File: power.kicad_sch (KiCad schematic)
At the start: 7 parts

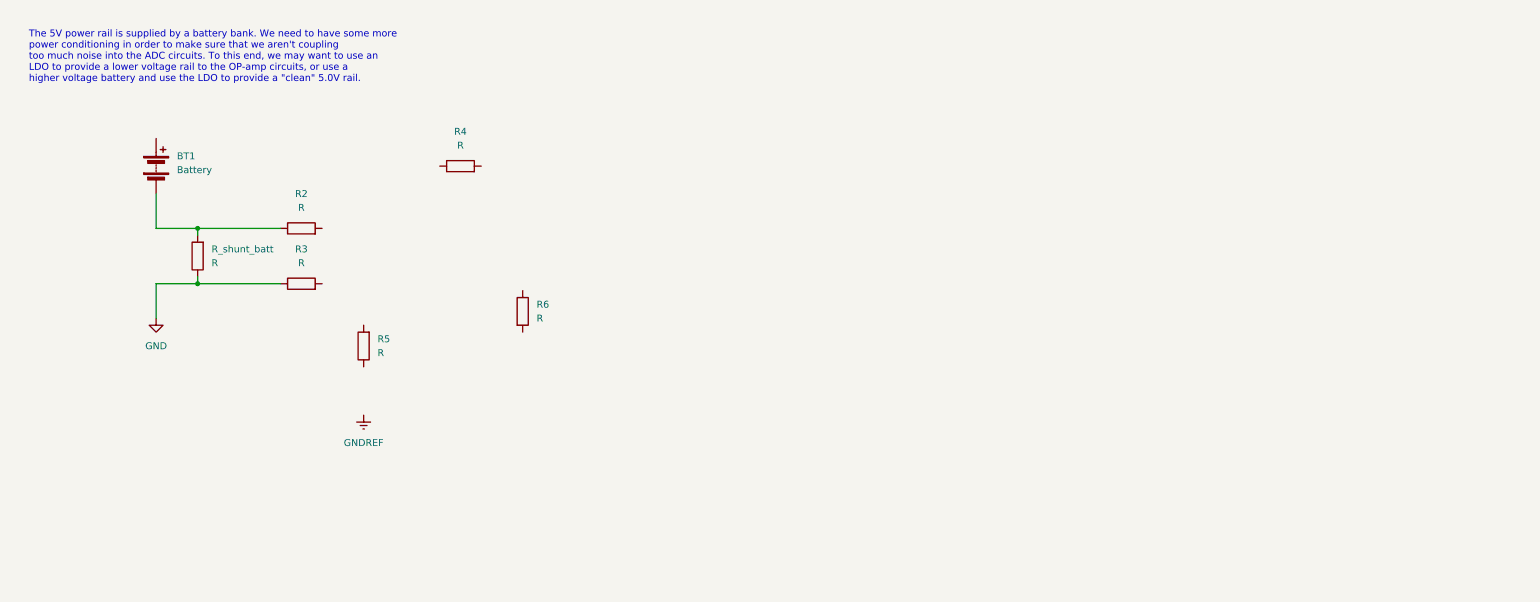
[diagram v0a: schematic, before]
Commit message: Split the sensor modules into a 4 and 8 port version. Fleshed out the power module a bit more. Started adding sensor board connectors to the root schematic and started pulling out sensor boards to their own, separate module. Began wiring up the root schematic to get my bearings a bit.
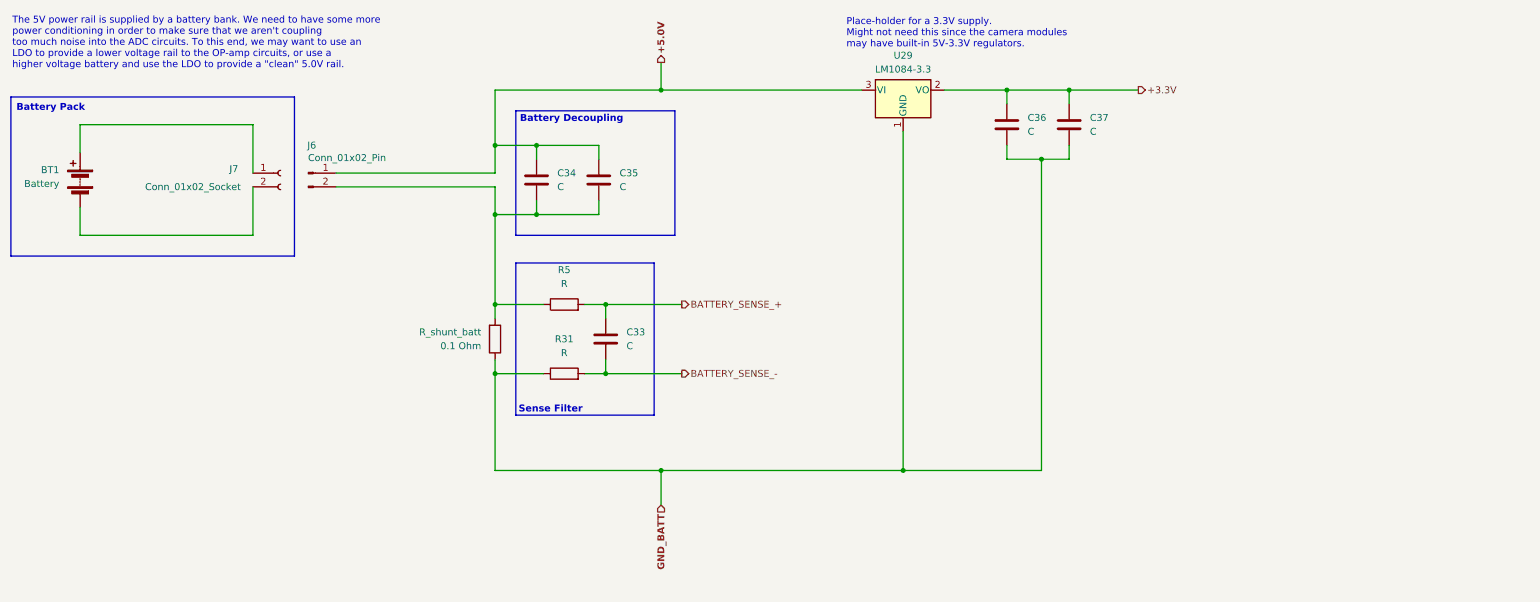
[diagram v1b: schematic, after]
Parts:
- removed R2, R3, R4, R6: R, symbol Device:R
- added C33, C34, C35, C36, C37: C, symbol Device:C
- added J6: Conn_01x02_Pin, symbol Connector:Conn_01x02_Pin
- added J7: Conn_01x02_Socket, symbol Connector:Conn_01x02_Socket
- added R31: R, symbol Device:R
- added U29: LM1084-3.3, symbol Regulator_Linear:LM1084-3.3
- R_shunt_batt: value R -> 0.1 Ohm
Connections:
- net at R_shunt_batt.2: now also R5.1, C34.2, C35.2, J6.2 (Pin_2); no longer BT1.2 (-)
- net at BT1.1 (+): now also J7.1 (Pin_1)
- net BATTERY_SENSE_+: now reaches R5.2
- net BATTERY_SENSE_+: now also C33.1
- net GND renamed GND_BATT
- net GND_BATT: now also C36.2, C37.2, R31.1, U29.1 (GND)
- new net: BT1.2 (-), J7.2 (Pin_2)
- new net +3.3V: C36.1, C37.1, U29.2 (VO)
- new net +5.0V: C34.1, C35.1, J6.1 (Pin_1), U29.3 (VI)
- new net BATTERY_SENSE_-: C33.2, R31.2
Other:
- note added: "Battery Decoupling"
- note added: "Battery Pack"
- note added: "Place-holder for a 3.3V supply. Might not need this since the camera modules may have built-in 5V-3.3V regulators."
- note added: "Sense Filter"
- moved on the sheet: BT1, R_shunt_batt

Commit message: More notes and comments Cleaned up some signal lines Compacted the decoupling sections Added Turbidity placeholder
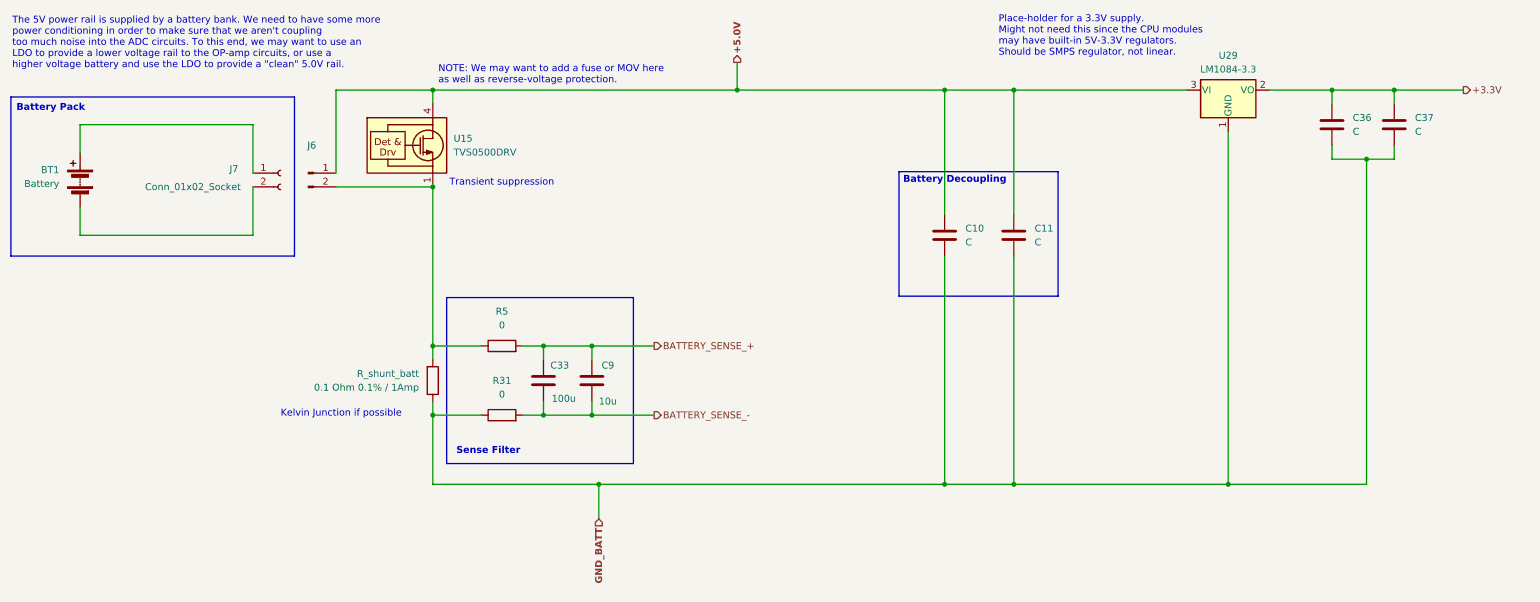
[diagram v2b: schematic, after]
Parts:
- removed C34, C35: C, symbol Device:C
- added C10, C11: C, symbol Device:C
- added C9: 10u, symbol Device:C
- added U15: TVS0500DRV, Package_SON:WSON-6-1EP_2x2mm_P0.65mm_EP1x1.6mm, symbol Power_Protection:TVS0500DRV
- C33: value C -> 100u
- R31, R5: value R -> 0
- R_shunt_batt: value 0.1 Ohm -> 0.1 Ohm 0.1% / 1Amp
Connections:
- net +5.0V: now also C10.1, C11.1, U15.4 (IN), U15.5 (IN), U15.6 (IN)
- net BATTERY_SENSE_+: now also C9.1
- net BATTERY_SENSE_-: now also C9.2
- net GND_BATT: now also C10.2, C11.2
- net at J6.2 (Pin_2), R5.1, R_shunt_batt.2: now also U15.1 (GND), U15.2 (GND), U15.3 (GND), U15.7 (GND)
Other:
- note added: "Kelvin Junction if possible"
- note added: "NOTE: We may want to add a fuse or MOV here as well as reverse-voltage protection."
- note added: "Place-holder for a 3.3V supply. Might not need this since the CPU modules may have built-in 5V-3.3V regulators. Should be SMPS regulator, not linear."
- note added: "Transient suppression"
- note removed: "Place-holder for a 3.3V supply. Might not need this since the camera modules may have built-in 5V-3.3V regulators."
- moved on the sheet: C33, C36, C37, R31, R5, R_shunt_batt, U29

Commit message: Cleaned up a bit Added a SPDT to calibrate signal on the base board Added PTC and MOV to power section
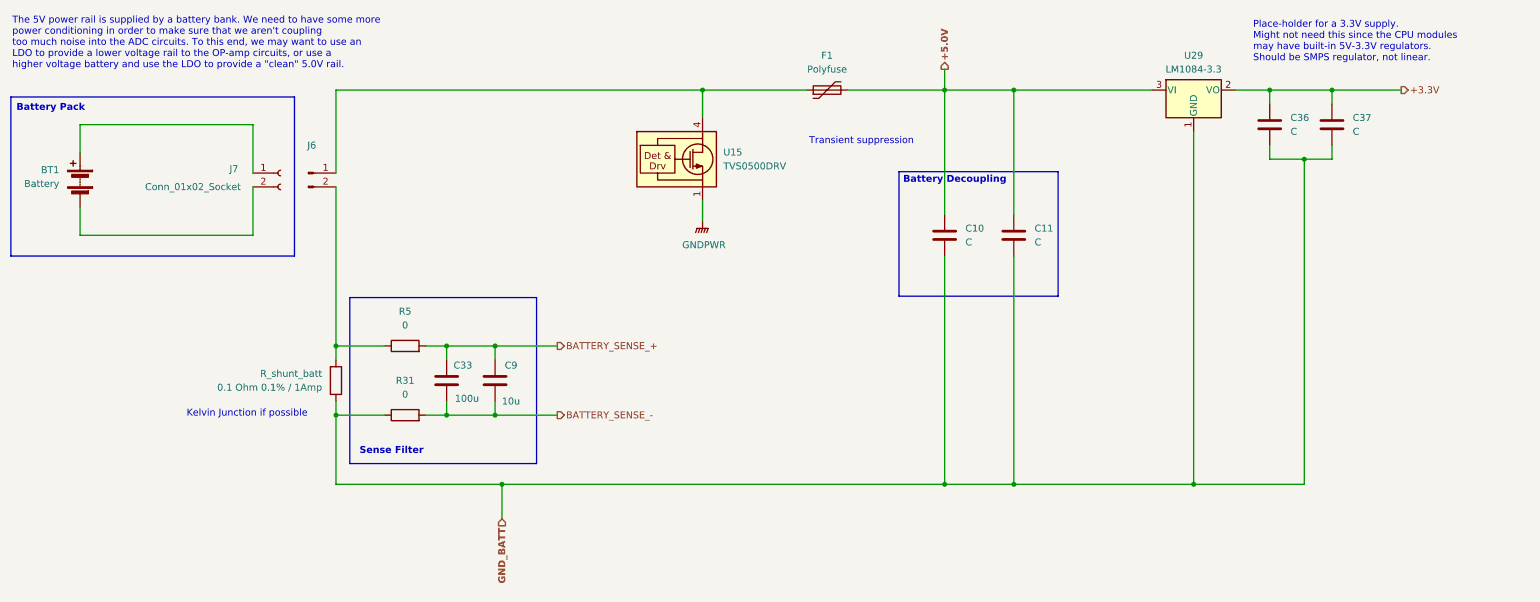
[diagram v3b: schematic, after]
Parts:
- added F1: Polyfuse, symbol Device:Polyfuse
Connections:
- net +5.0V: now also F1.2; no longer J6.1 (Pin_1), U15.4 (IN), U15.5 (IN), U15.6 (IN)
- net GNDPWR: now reaches U15.1 (GND), U15.2 (GND), U15.3 (GND), U15.7 (GND)
- net GNDPWR: no longer J6.2 (Pin_2), R5.1, R_shunt_batt.2
- new net: J6.2 (Pin_2), R5.1, R_shunt_batt.2
- new net: F1.1, J6.1 (Pin_1), U15.4 (IN), U15.5 (IN), U15.6 (IN)
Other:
- note removed: "NOTE: We may want to add a fuse or MOV here as well as reverse-voltage protection."
- moved on the sheet: C33, C36, C37, C9, R31, R5, R_shunt_batt, U29

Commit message: Began assigning footprints Cleaned up some of the signalling and added the full prototype sensor suite Added a header for the Atlas Scientific carrier board Added some test points and jumpers Cleaned up the power section Started work on the CPU signal assignment and header sockets
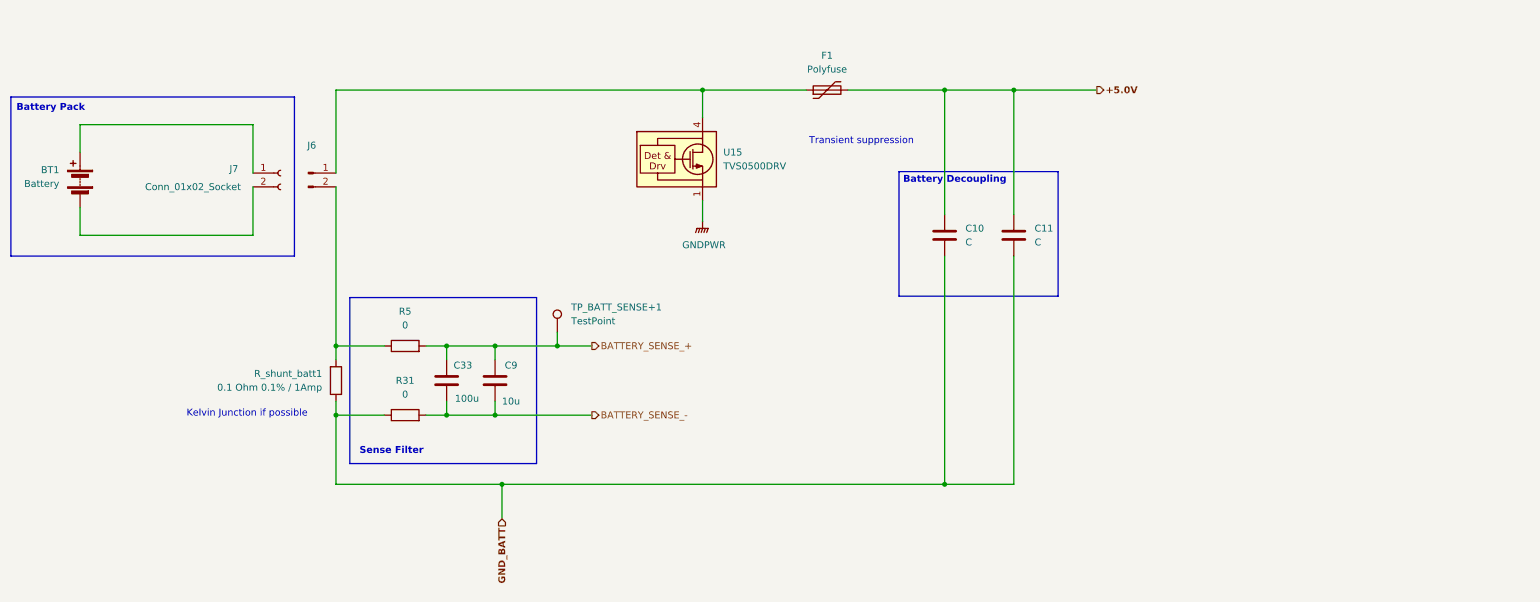
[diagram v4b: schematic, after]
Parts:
- removed C36, C37: C, symbol Device:C
- removed U29: LM1084-3.3, symbol Regulator_Linear:LM1084-3.3
- added TP_BATT_SENSE+1: TestPoint, symbol Connector:TestPoint
- renumbered R_shunt_batt to R_shunt_batt1
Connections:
- net BATTERY_SENSE_+: now also TP_BATT_SENSE+1.1
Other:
- note removed: "Place-holder for a 3.3V supply. Might not need this since the CPU modules may have built-in 5V-3.3V regulators. Should be SMPS regulator, not linear."
- note removed: "The 5V power rail is supplied by a battery bank. We need to have some more power conditioning in order to make sure that we aren't coupling too much noise into the ADC circuits. To this end, we may want to use an LDO to provide a lower voltage rail to the OP-amp circuits, or use a higher voltage battery and use the LDO to provide a "clean" 5.0V rail."
